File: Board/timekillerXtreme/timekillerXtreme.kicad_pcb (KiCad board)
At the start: 2 copper layers, 61.5 x 105.8 mm, 100 parts, among them J1 Battery, J10 Conn_01x02, J11 TP_USB, J12 PROG, J13 CONN_01X03, J14 TP_3.3V, J15 PE7, J16 PE8, J17 PE9, J18 PE10, J19 PD4, J2 USB_OTG, J20 PD1, J21 PD0, J22 PD3, J23 PE11, J24 Pb12, J3 Conn_Bottom_Expansion, J4 Conn_Internal_Expansion, J5 Conn_LCD_Board, J6 uSD, J7 CAPTEST, J8 TP_AUDIO_R, J9 TP_AUDIO_L, Q1 IRLML6302, Q2 PMBT3904.215, SW1 PWR, SW2 A, SW3 B, SW4 LEFT, SW5 RIGHT, SW6 DOWN, SW7 UP, SW8 RST, U1 MCP73831, U2 FT230XS-R, U3 NCP1529, U5 STM32F407VGT6, U6 USBLC6, U7 AOZ1310, U8 USBLC6, U9 USBLC6, Y1 32.768 KHz, Y2 16MHz

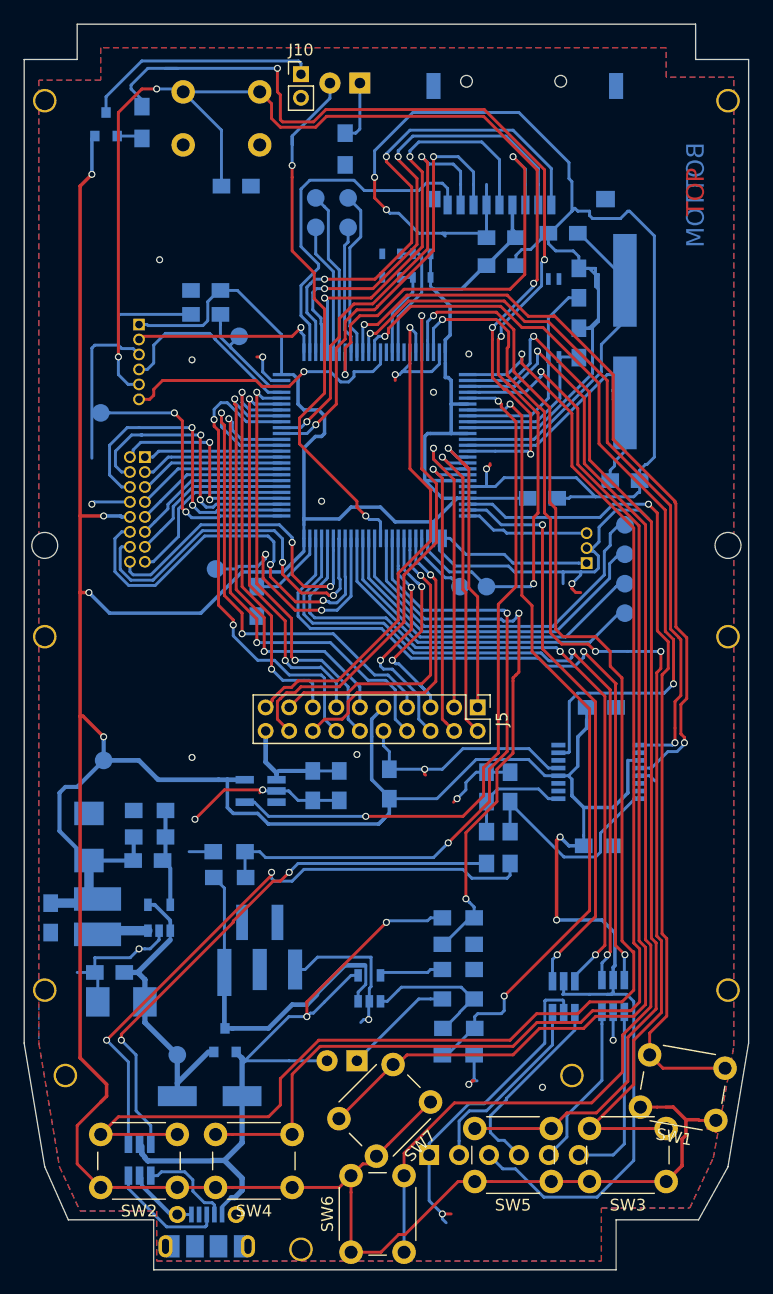
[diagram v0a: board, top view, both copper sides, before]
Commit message: Board: SD slot moved, usb-conn changed from slots to holes. LCD board polished. Repo cleaned up.
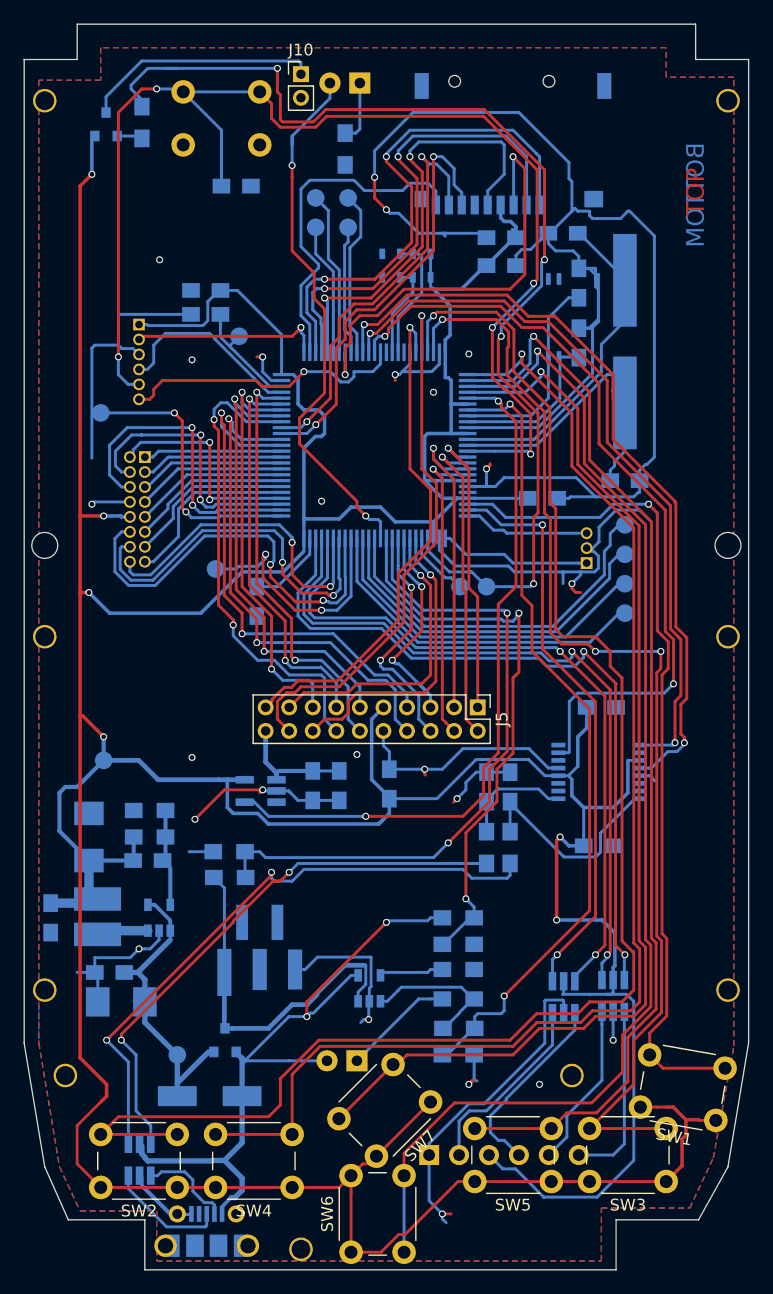
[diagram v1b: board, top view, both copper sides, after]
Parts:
- J2: footprint Connectors_USB:USB_Micro-B_Molex-105017-0001 -> timekiller-footprints:USB_Micro-B-CircularHoles
- moved J6 1.00 mm to (159.0, 55.4)
- moved J2 0.05 mm to (133.0, 143.3)
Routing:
- net GND: track 321.3 -> 317.2 mm
- net SD_CK: track 35.8 -> 37.5 mm
- net +3V3: track 471.4 -> 472.9 mm
- net SD_D1: track 36.9 -> 35.7 mm
- net SD_D0: track 37.7 -> 36.5 mm
- net SD_DETECT: track 30.4 -> 29.2 mm
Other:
- outline, holes or cut-outs redrawn

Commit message: pcbs polished a bit. Case bottom pcb clearance enlarged.
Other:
- board text added: "SDA-Wonder Beta 2018-09-03"
- board text removed: "SDA-Wonder Beta 2018-09-01"
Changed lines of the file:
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@@
     (links 254)
     (no_connects 11)
-    (area 117.449999 39.949999 179.050001 145.800001)
+    (area 109.692857 24.55 204.688599 149.60881)
     (thickness 1.6)
     (drawings 41)
@@
     (pad_drill 1.6)
     (pad_to_mask_clearance 0)
-    (aux_axis_origin 0 0)
+    (aux_axis_origin 117.5 39.75)
     (visible_elements FFFFEF7F)
     (pcbplotparams
@@
       (viasonmask false)
       (mode 1)
-      (useauxorigin false)
+      (useauxorigin true)
       (hpglpennumber 1)
       (hpglpenspeed 20)
@@
     (effects (font (size 1.5 1.5) (thickness 0.3)) (justify mirror))
   )
-  (gr_text "SDA-Wonder\nBeta 2018-09-01" (at 132.75 95.75 270) (layer B.SilkS)
+  (gr_text "SDA-Wonder\nBeta 2018-09-03" (at 132.75 95.75 270) (layer B.SilkS)
     (effects (font (size 1.5 1.5) (thickness 0.3)) (justify mirror))
   )

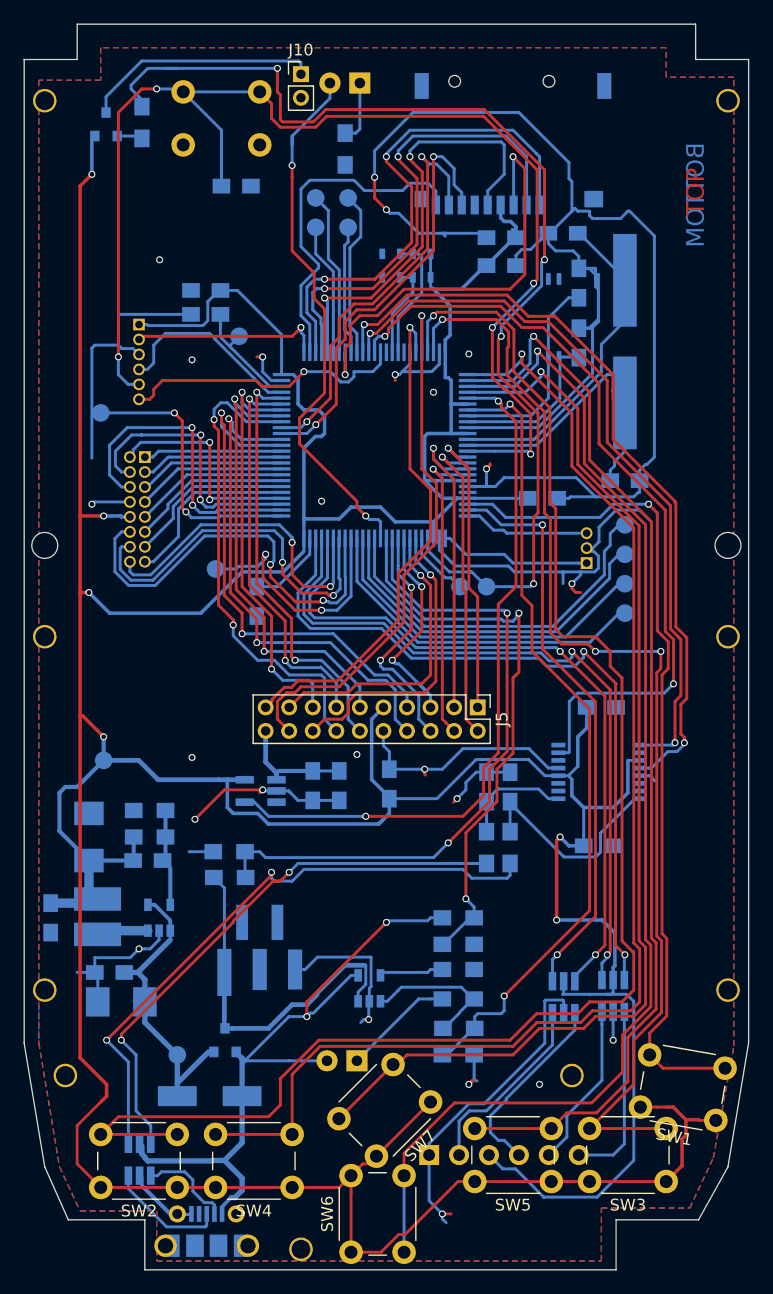
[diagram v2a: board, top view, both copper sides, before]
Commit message: Daily commit 3.9.2018: sd moved to the right position (hopefully). minor case tweaks.
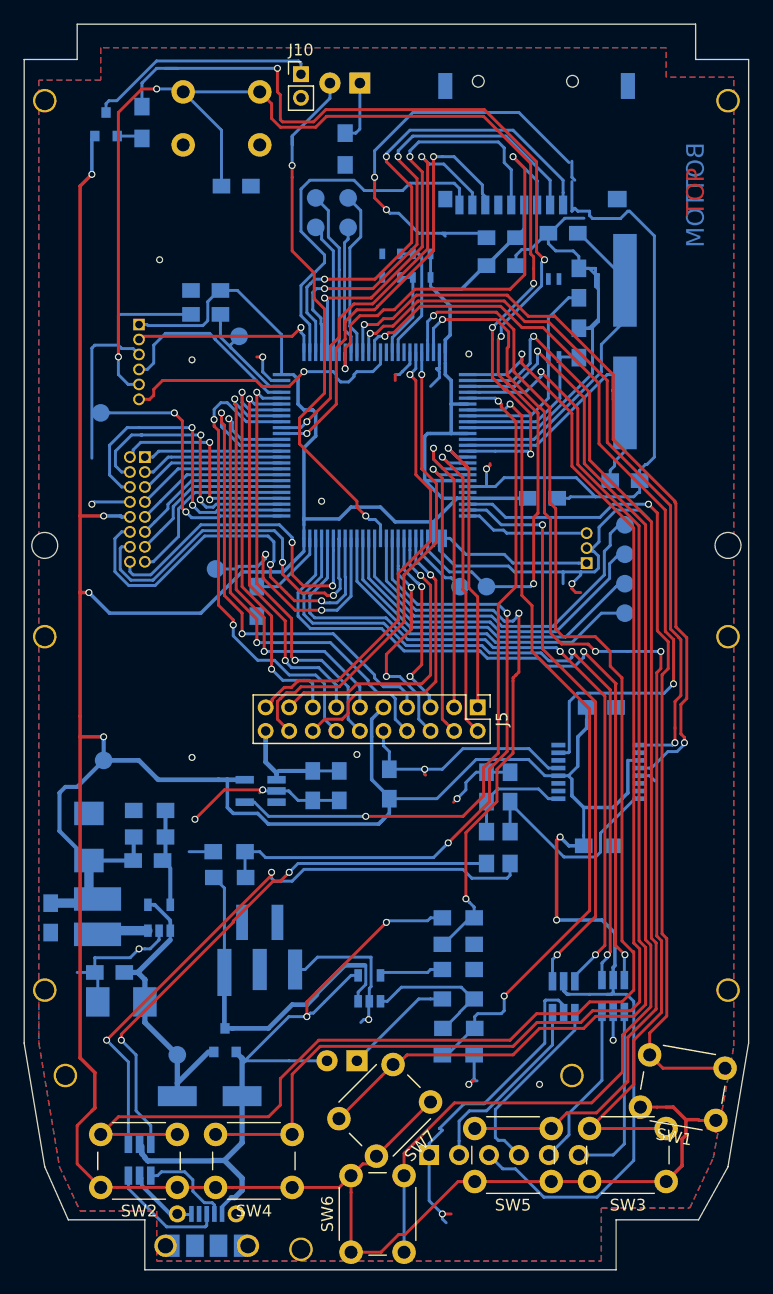
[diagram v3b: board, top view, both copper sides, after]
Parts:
- moved J6 2.00 mm to (161.0, 55.4)
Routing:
- net TS_P1: track 47.2 -> 41.0 mm
- net +3V3: track 472.9 -> 468.7 mm
- net TS_P2: track 43.5 -> 39.3 mm
- net LCD_D4: track 18.8 -> 16.1 mm
- net SD_DETECT: track 29.2 -> 31.8 mm
- net SD_D0: track 36.5 -> 37.9 mm
- net AUDIO_L: track 96.0 -> 94.8 mm
- net GND: track 317.2 -> 318.4 mm, vias 24 -> 22
- net SD_D1: track 35.7 -> 36.9 mm
- net SD_D3: track 40.8 -> 41.6 mm
- net SD_D2: track 43.6 -> 44.4 mm
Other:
- board text added: "SDA-Wonder Beta 2018-09-04"
- board text removed: "SDA-Wonder Beta 2018-09-03"

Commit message: SD card slot moved a bit again.
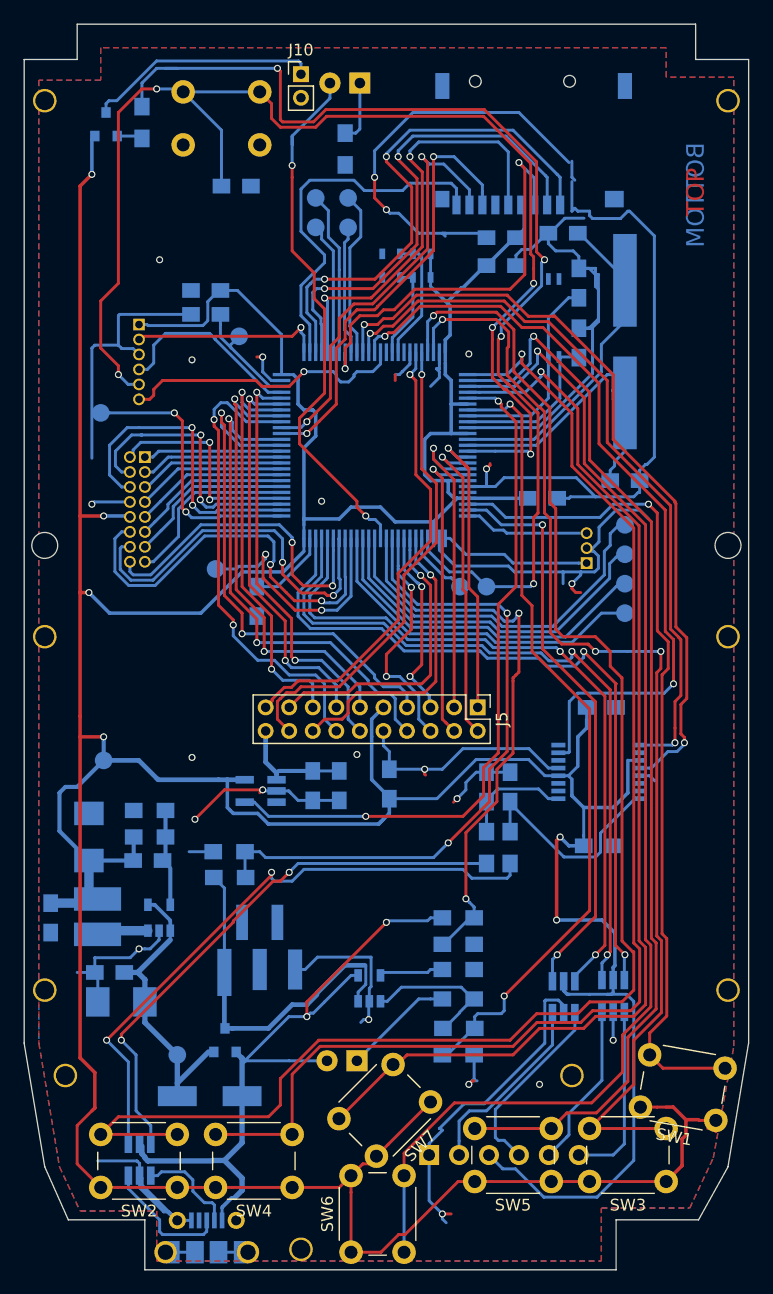
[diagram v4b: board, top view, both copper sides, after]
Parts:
- moved J2 0.55 mm to (133.0, 143.9)
- moved J6 0.25 mm to (160.8, 55.4)
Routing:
- net GND: track 318.4 -> 334.7 mm
- net +3V3: track 468.7 -> 466.5 mm
- net USB_VBUS: track 61.0 -> 62.6 mm
- net SD_CMD: track 37.3 -> 35.7 mm
- net RESET: track 106.8 -> 108.0 mm
- net Net-(J2-Pad3): track 10.1 -> 11.0 mm
- net Net-(J2-Pad2): track 8.07 -> 8.57 mm

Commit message: system board polished, lcd flex connector footprint updated.
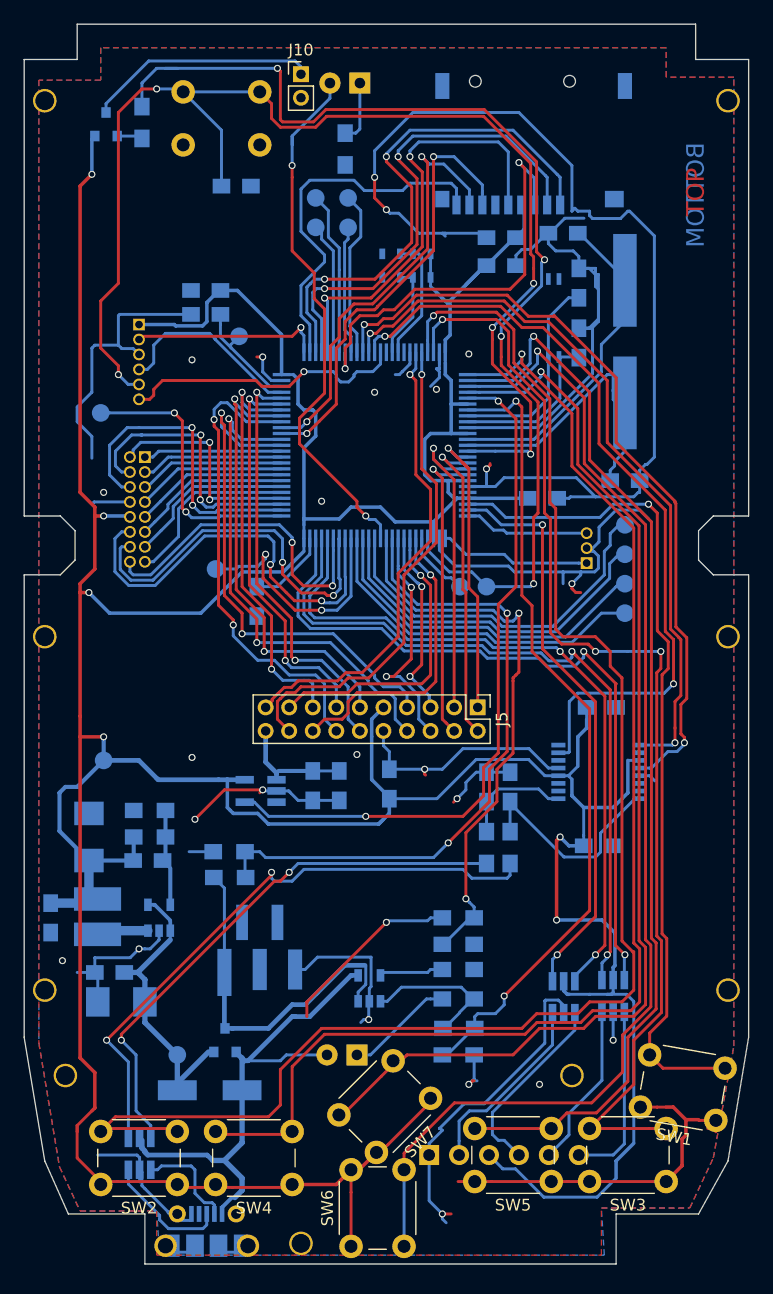
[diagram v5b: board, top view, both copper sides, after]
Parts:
- removed REF** (x2): MountingHole_2.2mm_M2, Mounting_Holes:MountingHole_2.2mm_M2
- moved J2 0.55 mm to (133.0, 143.3)
- moved ? 0.50 mm to (141.0, 143.5)
- moved D1 0.50 mm to (145.8, 127.5)
- moved D2 0.50 mm to (133.2, 130.5)
- moved SW6 0.50 mm to (145.2, 143.8)
- moved U6 0.50 mm to (127.3, 135.9)
- moved SW7 0.32 mm to (152.0, 131.2)
- moved SW2 0.25 mm to (130.5, 138.5)
- moved SW4 0.25 mm to (140.2, 138.5)
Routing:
- net +3V3: track 466.5 -> 458.4 mm
- net GND: track 334.7 -> 331.3 mm, vias 22 -> 23
- net TS_P1: track 41.0 -> 42.0 mm
- net Net-(J2-Pad2): track 8.57 -> 9.39 mm
- net TS_P2: track 39.2 -> 40.0 mm
- net USB_D-: track 47.4 -> 46.8 mm
- net USB_VBUS: track 62.6 -> 62.8 mm, vias 2 -> 1
- net (no net): vias 0 -> 1
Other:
- board size 61.5 x 105.8 mm -> 61.5 x 105.2 mm

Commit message: Silkscreen fixed. Some minor tweaks.
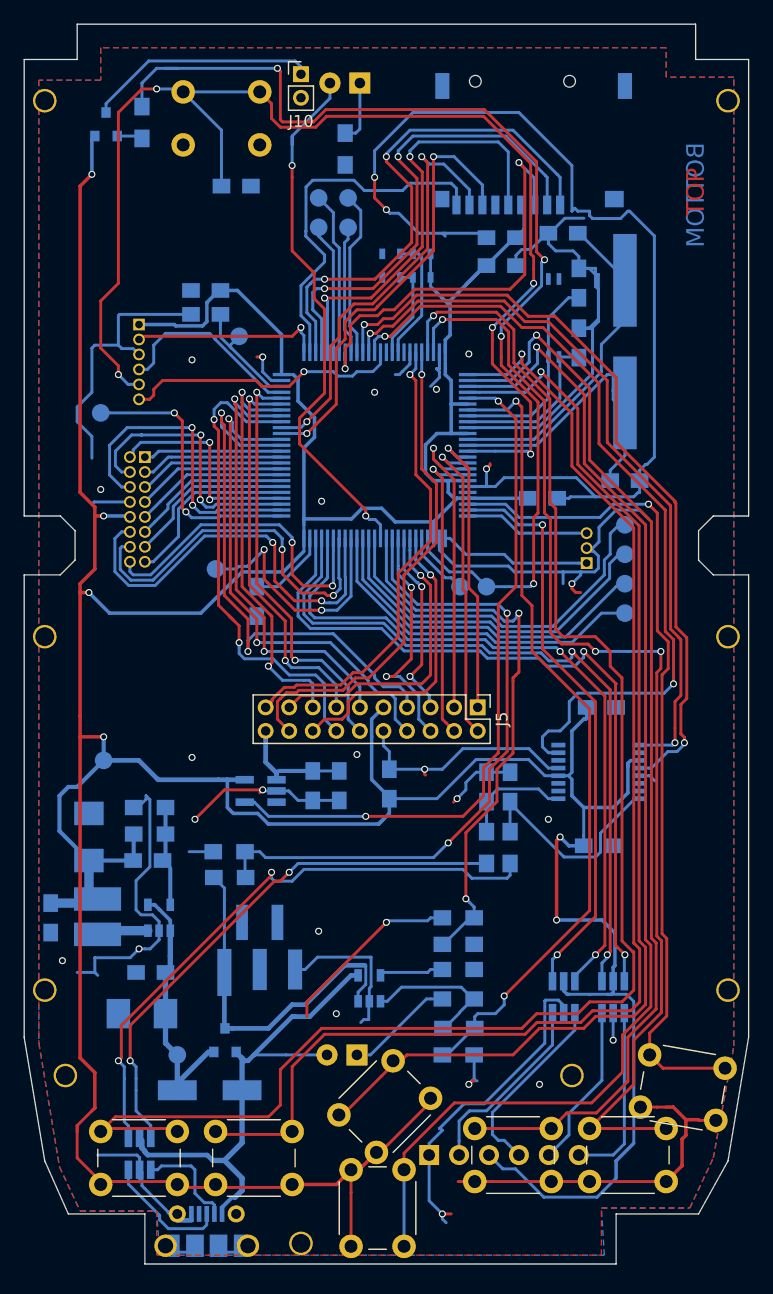
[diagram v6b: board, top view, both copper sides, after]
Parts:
- J3: footprint Pin_Headers:Pin_Header_Angled_1x06_Pitch2.54mm -> timekiller-footprints:Pin_Header__1x06_Pitch2.54mm-NoSilk
- moved C3 3.50 mm to (128.2, 120.5)
- moved C6 2.02 mm to (127.5, 124.0)
- moved J20 0.25 mm to (142.5, 54.8)
- moved J21 0.25 mm to (142.5, 57.2)
- moved R8 0.25 mm to (128.2, 108.8)
- moved R9 0.25 mm to (128.2, 106.5)
- moved U8 0.10 mm to (167.5, 122.6)
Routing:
- net GND: track 331.3 -> 344.2 mm, vias 23 -> 25
- net Net-(C3-Pad1): track 26.3 -> 22.2 mm
- net LCD_D6: track 44.1 -> 46.4 mm
- net FT23_TXE: track 66.8 -> 68.5 mm
- net USB_D+: track 52.3 -> 51.0 mm
- net +3V3: track 458.4 -> 457.1 mm
- net LCD_RS: track 40.6 -> 41.7 mm
- net BTN_2_DOWN: track 103.8 -> 104.8 mm
- net USB_VBUS: track 62.8 -> 62.1 mm
- net SWO_SWO: track 24.4 -> 23.8 mm
- net USB_D-: track 46.8 -> 46.2 mm
- net Net-(J21-Pad1): track 11.2 -> 11.8 mm
